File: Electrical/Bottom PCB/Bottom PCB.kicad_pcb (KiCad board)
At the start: 2 copper layers, 100 x 80 mm, 50 parts, among them J1 Steper1, J2 Steper2, J3 H Bridge, J5 Servo1, J6 Servo2, J7 Servo3, J8 MainIO, J9 Servo4, SW1 FL, SW2 FR, U1 ULN2003A, U10 MCP23017_SO, U2 74HC595, U3 QRE1113, U4 TB6612FNG, U5 74HC595, U6 QRE1113, U7 QRE1113, U8 QRE1113, U9 ESP32-WROVER

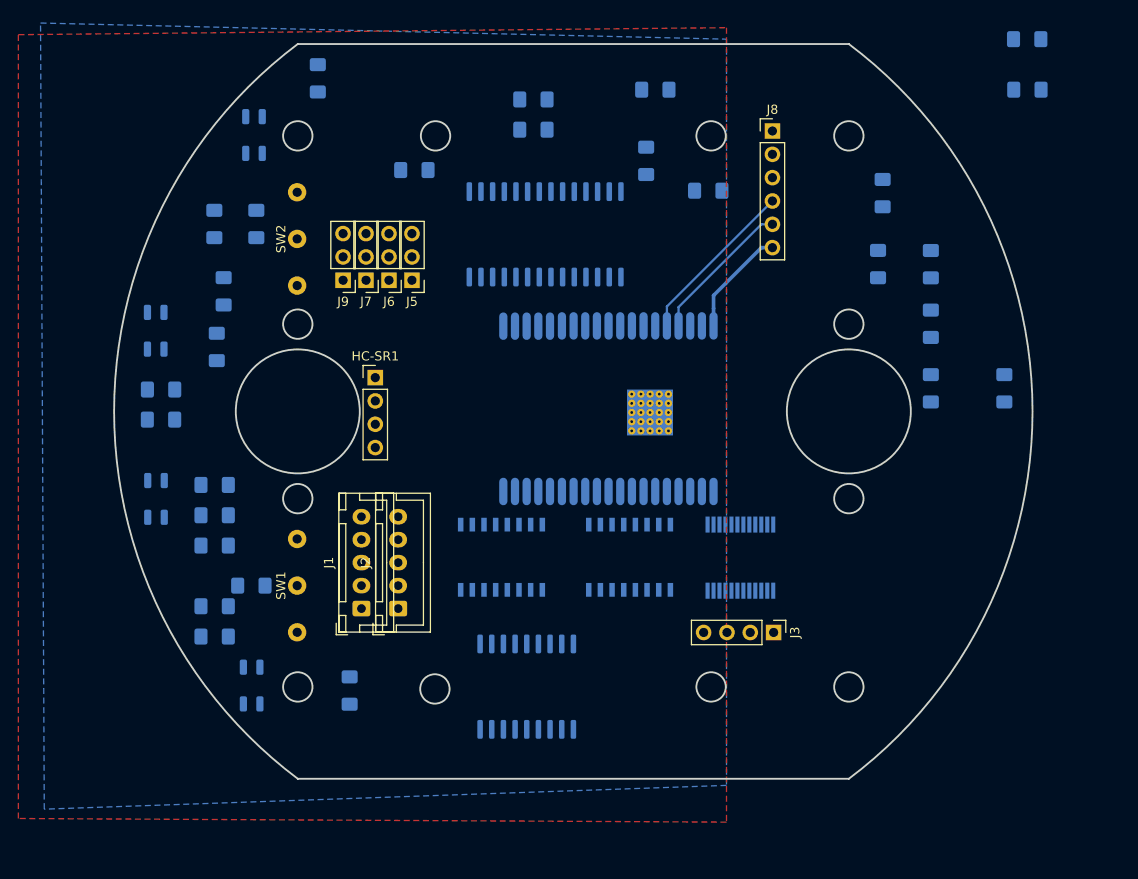
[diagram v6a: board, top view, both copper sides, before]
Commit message: Moved components to sub sheets
Continued on from Bob's work, in so much that I moved some items to additional sheets, increesed the size of the main header to include a half battery tap, and the addition of jumpers so that the device can be re-programmed without disasembly (however will need a soldering iron). may change this to a three way jumper at a later date,
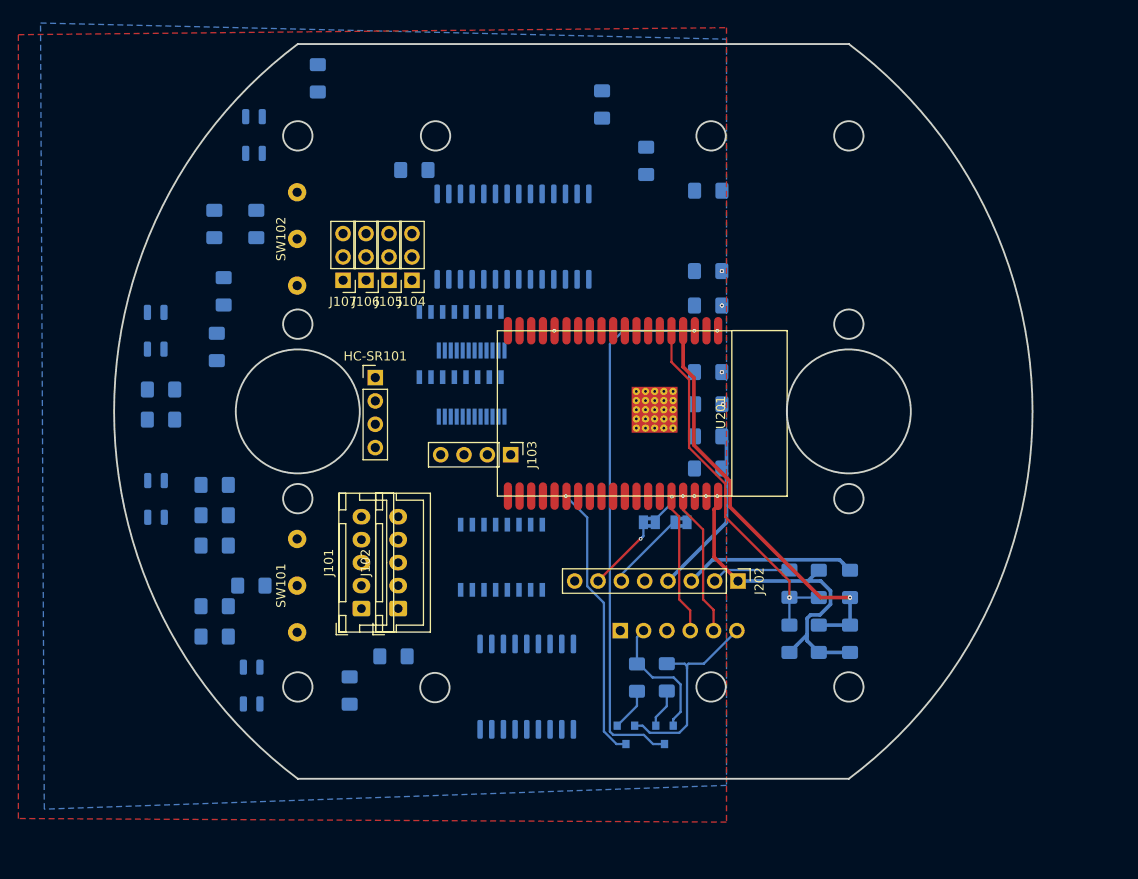
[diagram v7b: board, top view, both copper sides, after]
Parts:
- removed C14, C19, C2: 100pF, Capacitor_SMD:C_1206_3216Metric_Pad1.42x1.75mm_HandSolder
- removed C18, C3, C6, C8: 10uF, Capacitor_SMD:C_1206_3216Metric_Pad1.42x1.75mm_HandSolder
- removed J8: MainIO, Connector_PinHeader_2.54mm:PinHeader_1x06_P2.54mm_Vertical
- removed R1: 22k, Resistor_SMD:R_1206_3216Metric_Pad1.42x1.75mm_HandSolder
- removed R2: 10k, Resistor_SMD:R_1206_3216Metric_Pad1.42x1.75mm_HandSolder
- removed U5: 74HC595, Package_SO:SOIC-16W_5.3x10.2mm_P1.27mm
- removed U9: ESP32-WROVER, esp32-wrover:ESP32-WROVER
- added C104: 10uF, Capacitor_SMD:C_1206_3216Metric_Pad1.42x1.75mm_HandSolder, B.Cu at (163.8, 95.8)
- added C108: 100pF, Capacitor_SMD:C_1206_3216Metric_Pad1.42x1.75mm_HandSolder, B.Cu at (163.8, 92.2)
- added C201: 10uF, Capacitor_SMD:C_1206_3216Metric_Pad1.42x1.75mm_HandSolder, B.Cu at (163.8, 78.0)
- added C202: 10uF, Capacitor_SMD:C_1206_3216Metric_Pad1.42x1.75mm_HandSolder, B.Cu at (163.8, 74.2)
- added C203: 100pF, Capacitor_SMD:C_1206_3216Metric_Pad1.42x1.75mm_HandSolder, B.Cu at (163.8, 85.2)
- added C204: 100pF, Capacitor_SMD:C_1206_3216Metric_Pad1.42x1.75mm_HandSolder, B.Cu at (163.8, 88.8)
- added C301: 10uF, Capacitor_SMD:C_1206_3216Metric_Pad1.42x1.75mm_HandSolder, B.Cu at (175.8, 114.3)
- added C302: 10uF, Capacitor_SMD:C_1206_3216Metric_Pad1.42x1.75mm_HandSolder, B.Cu at (175.8, 108.3)
- added J201: PROGRAMMING, Connector_PinHeader_2.54mm:PinHeader_1x06_P2.54mm_Vertical, B.Cu at (154.2, 113.4)
- added J202: MainIO, Connector_PinHeader_2.54mm:PinHeader_1x08_P2.54mm_Vertical, F.Cu at (167.0, 108.0)
- added JP201: Jumper_2_Bridged, Jumper:SolderJumper-2_P1.3mm_Bridged2Bar_Pad1.0x1.5mm, B.Cu at (160.8, 101.6)
- added JP202: Jumper_2_Bridged, Jumper:SolderJumper-2_P1.3mm_Bridged2Bar_Pad1.0x1.5mm, B.Cu at (157.3, 101.6)
- added Q201: BC847, Package_TO_SOT_SMD:SOT-23, B.Cu at (159.0, 124.8)
- added Q202: BC847, Package_TO_SOT_SMD:SOT-23, B.Cu at (154.8, 124.8)
- added R201: 10K, Resistor_SMD:R_1206_3216Metric_Pad1.42x1.75mm_HandSolder, B.Cu at (159.2, 118.5)
- added R202: 10K, Resistor_SMD:R_1206_3216Metric_Pad1.42x1.75mm_HandSolder, B.Cu at (156.0, 118.5)
- added R301: 22k, Resistor_SMD:R_1206_3216Metric_Pad1.42x1.75mm_HandSolder, B.Cu at (179.2, 108.3)
- added R302: 10k, Resistor_SMD:R_1206_3216Metric_Pad1.42x1.75mm_HandSolder, B.Cu at (179.2, 114.3)
- added R303: 22k, Resistor_SMD:R_1206_3216Metric_Pad1.42x1.75mm_HandSolder, B.Cu at (172.6, 108.3)
- added R304: 10k, Resistor_SMD:R_1206_3216Metric_Pad1.42x1.75mm_HandSolder, B.Cu at (172.6, 114.3)
- added U105: 74HC595, Package_SO:SOIC-16W_5.3x10.2mm_P1.27mm, B.Cu at (136.8, 82.2)
- added U201: ESP32-WROVER, esp32-wrover:ESP32-WROVER, F.Cu at (165.8, 89.8)
- moved C101 96.3 mm to (129.5, 116.2)
- moved U104 34.9 mm to (138.0, 86.5)
- moved J103 34.6 mm to (142.2, 94.2)
- moved C103 32.0 mm to (152.2, 56.1)
- moved Logo101 7.54 mm to (188.2, 113.8)
- moved U108 3.51 mm to (142.5, 70.5)
- renumbered C1 to C101, C4 to C102, C7 to C103, C9 to C105, C10 to C106, C13 to C107, C15 to C109, C16 to C110, C17 to C111, HC-SR1 to HC-SR101, J1 to J101, J2 to J102, J3 to J103, J5 to J104, J6 to J105, J7 to J106, J9 to J107, Logo1 to Logo101, R3 to R101, R4 to R102, R5 to R103, R6 to R104, R7 to R105, R8 to R106, R9 to R107, R10 to R108, R11 to R109, R12 to R110, SW1 to SW101, SW2 to SW102, U1 to U101, U2 to U102, U3 to U103, U4 to U104, U6 to U106, U7 to U107, U10 to U108, U8 to U109
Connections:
- J104 pad 1: Servo1 -> (no net)
- J105 pad 1: Servo2 -> (no net)
- J106 pad 1: Servo3 -> (no net)
- J107 pad 1: Servo4 -> (no net)
- SW101 pad 3: Net-(SW1-Pad3) -> (no net)
- SW102 pad 3: Net-(SW2-Pad3) -> (no net)
- U102 pad 14: DATA -> (no net)
- U104 pad 15: M2PWM -> (no net)
- U104 pad 23: M1PWM -> (no net)
- U108 pad 1: Net-(U10-Pad1) -> (no net)
- U108 pad 10: Net-(U10-Pad10) -> (no net)
- U108 pad 11: Net-(U10-Pad11) -> (no net)
- U108 pad 12: Net-(U10-Pad12) -> (no net)
- U108 pad 13: Net-(U10-Pad13) -> (no net)
- U108 pad 14: Net-(U10-Pad14) -> (no net)
- U108 pad 15: Net-(U10-Pad15) -> (no net)
- U108 pad 16: Net-(U10-Pad16) -> (no net)
- U108 pad 17: Net-(U10-Pad17) -> (no net)
- U108 pad 18: Net-(U10-Pad18) -> (no net)
- U108 pad 19: Net-(U10-Pad19) -> (no net)
- U108 pad 2: Net-(U10-Pad2) -> (no net)
- U108 pad 20: Net-(U10-Pad20) -> (no net)
- U108 pad 21: Net-(U10-Pad21) -> (no net)
- U108 pad 22: Net-(U10-Pad22) -> (no net)
- U108 pad 23: Net-(U10-Pad23) -> (no net)
- U108 pad 24: Net-(U10-Pad24) -> (no net)
- U108 pad 25: Net-(U10-Pad25) -> (no net)
- U108 pad 26: Net-(U10-Pad26) -> (no net)
- U108 pad 27: Net-(U10-Pad27) -> (no net)
- U108 pad 28: Net-(U10-Pad28) -> (no net)
- U108 pad 3: Net-(U10-Pad3) -> (no net)
- U108 pad 4: Net-(U10-Pad4) -> (no net)
- U108 pad 5: Net-(U10-Pad5) -> (no net)
- U108 pad 6: Net-(U10-Pad6) -> (no net)
- U108 pad 7: Net-(U10-Pad7) -> (no net)
- U108 pad 8: Net-(U10-Pad8) -> (no net)
- U108 pad 9: Net-(U10-Pad9) -> (no net)
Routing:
- net EN: track 0.00 -> 58.5 mm, vias 0 -> 1
- net BatV: track 0.00 -> 44.9 mm, vias 0 -> 1
- net half_BatV: track 0.00 -> 40.6 mm, vias 0 -> 1
- net GPIO0: track 0.00 -> 30.3 mm, vias 0 -> 1
- net GND: track 11.9 -> 37.7 mm, vias 0 -> 3
- net /ESP32-WROVER/DTR: track 0.00 -> 22.5 mm
- net +5V: track 0.00 -> 19.0 mm
- net +BATT: track 0.00 -> 18.7 mm
- net /ESP32-WROVER/CTS: track 0.00 -> 14.5 mm
- net /ESP32-WROVER/TX_sw: track 0.00 -> 8.91 mm
- net +3V8: track 0.00 -> 8.64 mm
- net /ESP32-WROVER/RX_sw: track 0.00 -> 8.47 mm, vias 0 -> 1
- net Net-(Q202-Pad1): track 0.00 -> 4.84 mm
- net Net-(Q201-Pad1): track 0.00 -> 4.27 mm
- net TX: track 16.0 -> 19.0 mm, vias 0 -> 1
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- added copper zone on F.Cu, net +3V3
- removed copper zone on F.Cu, net +5V
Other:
- outline, holes or cut-outs redrawn

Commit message: simplified the pcb,
Removed the shift registers and moved functionality onto the 16 way IO expander, also removed the H-Bridge, may re-add a I2C duel h-bridge at a later date.

Thinking about best way to drive the four servo headers, may use I2C controller for them as well, as then the timing maths is removed from the main micro
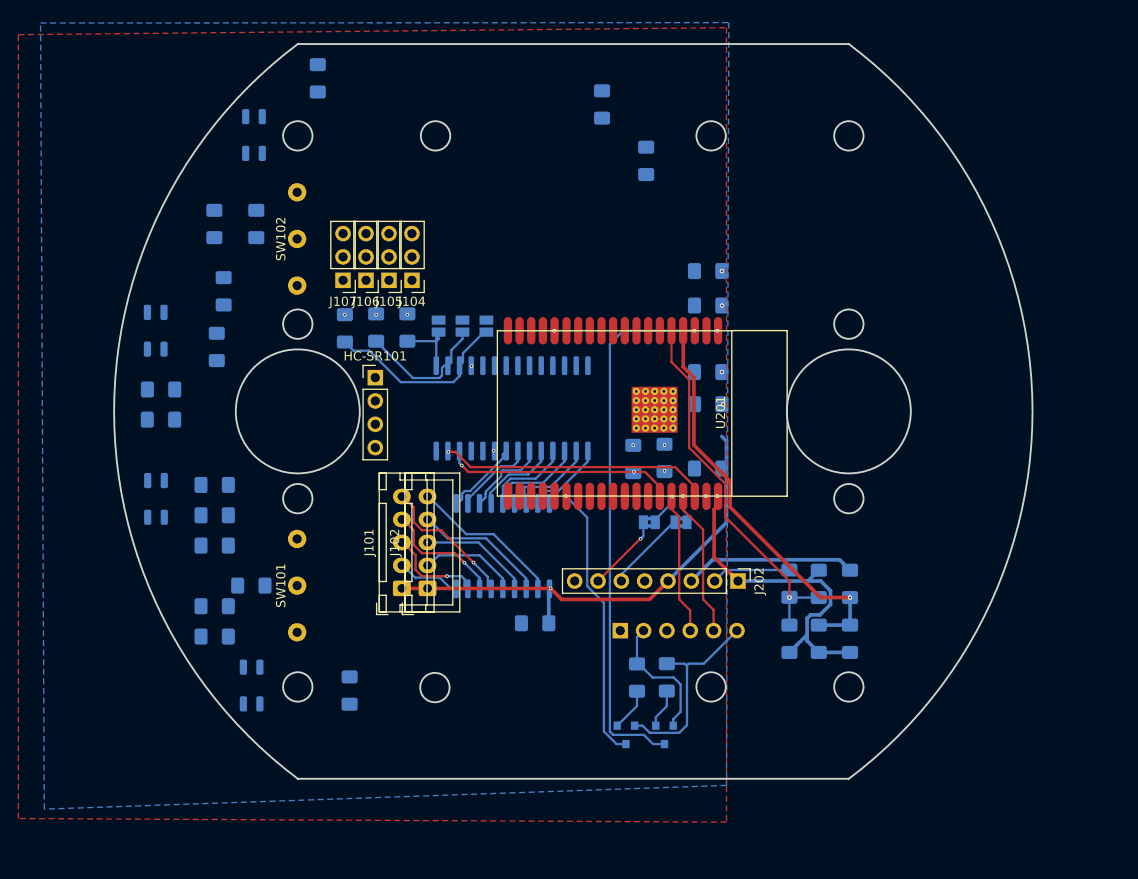
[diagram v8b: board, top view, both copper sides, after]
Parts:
- removed C105, C108: 100pF, Capacitor_SMD:C_1206_3216Metric_Pad1.42x1.75mm_HandSolder
- removed C106: 10uF, Capacitor_SMD:C_1206_3216Metric_Pad1.42x1.75mm_HandSolder
- removed J103: H Bridge, Connector_PinHeader_2.54mm:PinHeader_1x04_P2.54mm_Vertical
- removed U102, U105: 74HC595, Package_SO:SOIC-16W_5.3x10.2mm_P1.27mm
- removed U104: TB6612FNG, Package_SO:SSOP-24_5.3x8.2mm_P0.65mm
- added JP101: A2, Jumper:SolderJumper-2_P1.3mm_Open_Pad1.0x1.5mm, B.Cu at (139.6, 80.2)
- added JP102: A1, Jumper:SolderJumper-2_P1.3mm_Open_Pad1.0x1.5mm, B.Cu at (137.0, 80.2)
- added JP103: A0, Jumper:SolderJumper-2_P1.3mm_Open_Pad1.0x1.5mm, B.Cu at (134.4, 80.2)
- added R109: 4k7, Resistor_SMD:R_1206_3216Metric_Pad1.42x1.75mm_HandSolder, B.Cu at (124.2, 80.5)
- added R110: 4k7, Resistor_SMD:R_1206_3216Metric_Pad1.42x1.75mm_HandSolder, B.Cu at (127.6, 80.4)
- added R111: 4k7, Resistor_SMD:R_1206_3216Metric_Pad1.42x1.75mm_HandSolder, B.Cu at (131.0, 80.4)
- added R201: 4K7, Resistor_SMD:R_1206_3216Metric_Pad1.42x1.75mm_HandSolder, B.Cu at (159.0, 94.6)
- added R202: 4k7, Resistor_SMD:R_1206_3216Metric_Pad1.42x1.75mm_HandSolder, B.Cu at (155.6, 94.7)
- C102: value 100pF -> 10uF
- moved U107 18.7 mm to (142.4, 89.2)
- moved C101 15.8 mm to (144.9, 112.6)
- moved U101 15.5 mm to (141.4, 104.2)
- moved J101 4.92 mm to (130.4, 108.8)
- moved J102 3.88 mm to (133.2, 108.8)
- renumbered R109 to R112, R110 to R113, R201 to R203, R202 to R204, U108 to U107, U107 to U108
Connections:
- J104 pad 2: +5V -> Net-(J104-Pad2)
- J105 pad 2: +5V -> Net-(J104-Pad2)
- J106 pad 2: +5V -> Net-(J104-Pad2)
- J107 pad 2: +5V -> Net-(J104-Pad2)
- U107 pad 1: (no net) -> Net-(U101-Pad8)
- U107 pad 10: (no net) -> GND
- U107 pad 12: (no net) -> SCL
- U107 pad 13: (no net) -> SDA
- U107 pad 15: (no net) -> Net-(JP103-Pad1)
- U107 pad 16: (no net) -> Net-(JP102-Pad1)
- U107 pad 17: (no net) -> Net-(JP101-Pad1)
- U107 pad 18: (no net) -> +3V3
- U107 pad 2: (no net) -> Net-(U101-Pad7)
- U107 pad 3: (no net) -> Net-(U101-Pad6)
- U107 pad 4: (no net) -> Net-(U101-Pad5)
- U107 pad 5: (no net) -> Net-(U101-Pad4)
- U107 pad 6: (no net) -> Net-(U101-Pad3)
- U107 pad 7: (no net) -> Net-(U101-Pad2)
- U107 pad 8: (no net) -> Net-(U101-Pad1)
- U107 pad 9: (no net) -> +3V3
- U201 pad 33: (no net) -> SCL
- U201 pad 36: (no net) -> SDA
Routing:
- net +5V: track 19.0 -> 53.1 mm, vias 0 -> 1
- net SDA: track 0.00 -> 29.5 mm, vias 0 -> 2
- net SCL: track 0.00 -> 25.2 mm, vias 0 -> 2
- net Net-(JP101-Pad1): track 0.00 -> 20.7 mm
- net Net-(J102-Pad5): track 0.00 -> 16.8 mm
- net Net-(J101-Pad5): track 0.00 -> 15.4 mm, vias 0 -> 1
- net Net-(JP102-Pad1): track 0.00 -> 14.8 mm
- net Net-(J102-Pad4): track 0.00 -> 14.5 mm
- net Net-(J101-Pad4): track 0.00 -> 13.2 mm, vias 0 -> 1
- net Net-(J102-Pad3): track 0.00 -> 12.2 mm
- net Net-(J102-Pad2): track 0.00 -> 10.8 mm
- net Net-(J101-Pad3): track 0.00 -> 10.6 mm, vias 0 -> 1
- net Net-(U101-Pad6): track 0.00 -> 10.3 mm
- net Net-(U101-Pad7): track 0.00 -> 9.87 mm
- net Net-(U101-Pad5): track 0.00 -> 9.61 mm
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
